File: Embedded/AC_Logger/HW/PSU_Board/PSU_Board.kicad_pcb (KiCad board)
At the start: 2 copper layers, 99.1 x 40.6 mm, 17 parts, among them J1 Screw_Terminal_01x02, J2 NS25-W3P male, T1 230V 3.2VA - 2x 12V 1.6VA, U1 L7809, U2 L7909

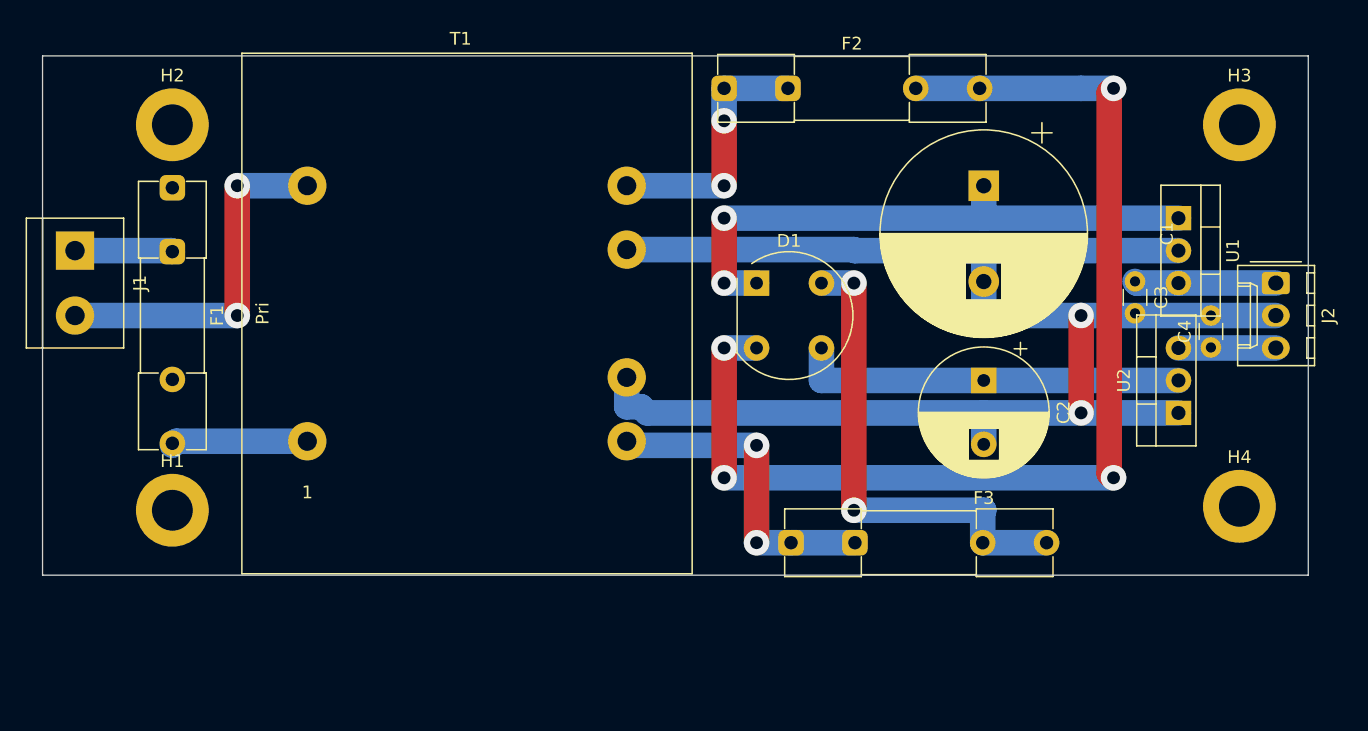
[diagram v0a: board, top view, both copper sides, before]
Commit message: PCB changed to make sandwitch.
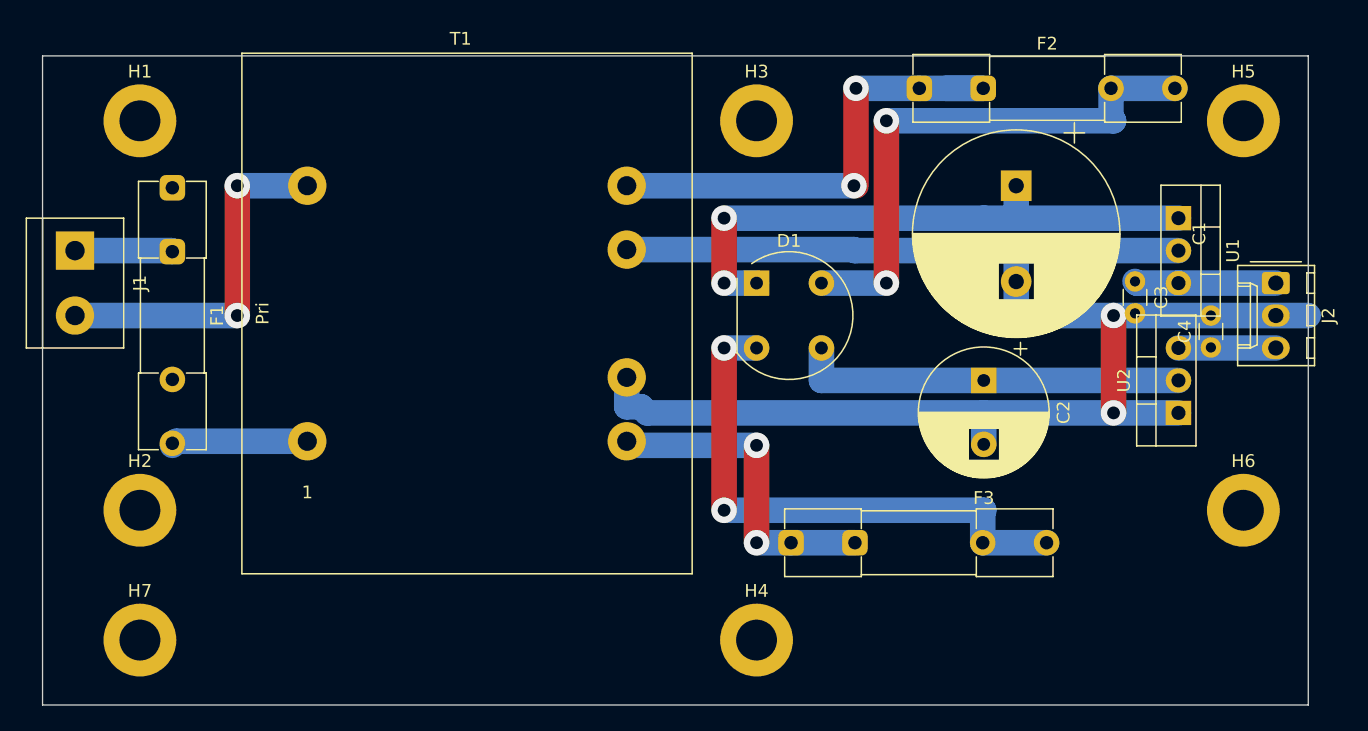
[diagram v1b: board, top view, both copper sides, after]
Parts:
- added H5: MountingHole, MountingHole:MountingHole_3.2mm_M3_ISO7380_Pad, F.Cu at (129.5, 55.9)
- added H6: MountingHole, MountingHole:MountingHole_3.2mm_M3_ISO7380_Pad, F.Cu at (129.5, 86.4)
- added H7: MountingHole, MountingHole:MountingHole_3.2mm_M3_ISO7380_Pad, F.Cu at (43.2, 96.5)
- moved H4 39.2 mm to (91.4, 96.5)
- moved H3 37.8 mm to (91.4, 55.9)
- moved H1 30.6 mm to (43.2, 55.9)
- moved H2 30.3 mm to (43.2, 86.4)
- moved F2 15.3 mm to (104.2, 53.3)
- moved C1 2.54 mm to (111.8, 61.0)
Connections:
- F2 pad 2: Net-(D1-Pad2) -> Net-(D1-Pad4)
- F3 pad 2: Net-(D1-Pad4) -> Net-(D1-Pad2)
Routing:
- net Net-(D1-Pad2): track 89.4 -> 43.1 mm, vias 4 -> 2
- net Net-(T1-SA): track 20.2 -> 38.3 mm
- net Net-(D1-Pad4): track 38.1 -> 43.2 mm
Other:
- board size 99.1 x 40.6 mm -> 99.1 x 50.8 mm

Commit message: Corrections.
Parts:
- moved C2 7.13 mm to (104.1, 81.2), turned to 90 degrees
- moved C3 0.86 mm to (121.9, 68.5)
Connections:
- C2 pad 1: Net-(D1--) -> GND
- C2 pad 2: GND -> Net-(D1--)
